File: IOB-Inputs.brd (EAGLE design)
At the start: 20.3 x 50.8 mm, 22 parts, among them J1 RJ12/6, Q0 P-FET, Q1 P-FET, Q2 P-FET, Q3 P-FET

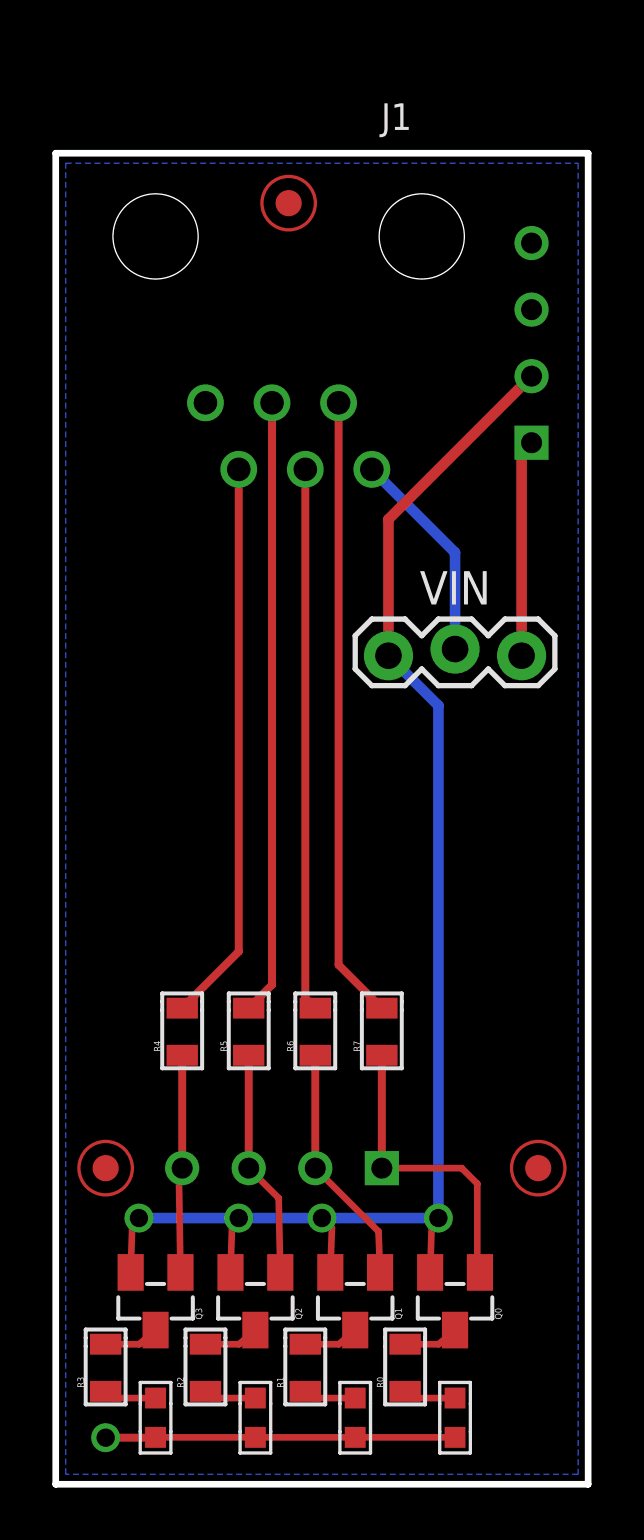
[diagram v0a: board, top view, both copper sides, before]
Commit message: added input protection diodes and RC filter to handle 1khz or less signals
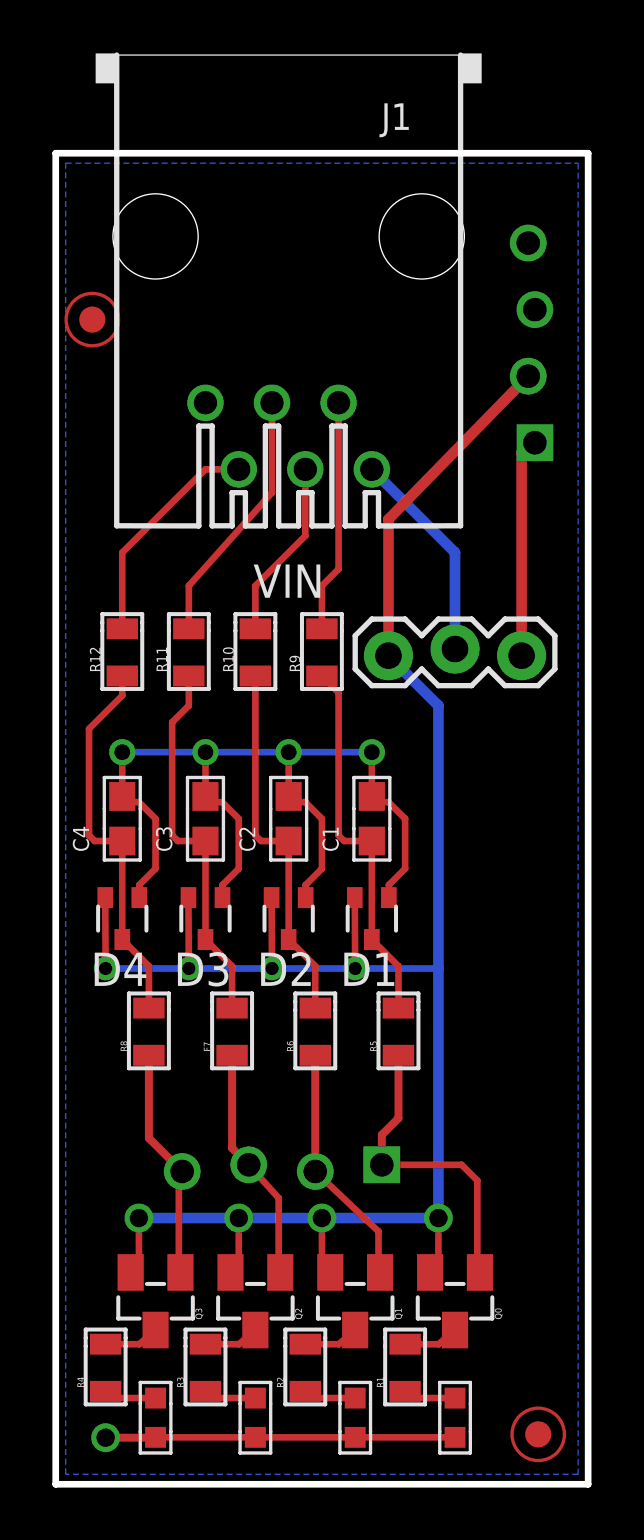
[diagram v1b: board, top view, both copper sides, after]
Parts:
- removed FID3: FIDUCIAL, SPCoast:FIDUCIAL_1MM
- removed LED0: Y, SPCoast:0603-LED
- removed R0: 2K0, SPCoast:0805-RES
- removed R7: 1K0, SPCoast:0805-RES
- added C1, C2, C3, C4: 0.01uF, SPCoast:0603-CAP
- added D1, D2, D3, D4: (no value), SPCoast:SOT323R
- added F7, R8: 1K0, SPCoast:0805-RES
- added LED4: Y, SPCoast:0603-LED
- added R10, R11, R12, R9: 82R, SPCoast:0805-RES
- IOB: value IO4-IOBBARE -> CONNECTOR-IO4-IOBBARE
- J1: device SPCoast:RJ25 -> SPCoast:RJ25-PANEL
- R4: value 1K0 -> 2K0
- moved R4 13.2 mm to (1.91, 4.45)
- moved FID2 10.2 mm to (18.4, 1.91)
- moved FID1 8.71 mm to (1.40, 44.5)
- moved R5 5.71 mm to (13.1, 17.3)
- moved LED1 3.81 mm to (15.2, 2.54)
- moved R1 3.81 mm to (13.3, 4.45)
- moved R2 3.81 mm to (9.53, 4.45)
- moved LED3 3.81 mm to (7.62, 2.54)
- moved LED2 3.81 mm to (11.4, 2.54)
- moved R3 3.81 mm to (5.71, 4.45)
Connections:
- removed net N$2 (its old number): LED0.A, R0.1
- new net N$10: C4.1, D4.2, R12.1, R8.2
- new net N$12: C3.1, D3.2, F7.2, R11.1
- new net N$13: C2.1, D2.2, R10.1, R6.2
- new net N$14: C1.1, D1.2, R5.2, R9.1
- new net N$5: LED4.A, R4.1
- net !IO1: now also R9.2; no longer R7.2
- net !IO2: now also R10.2; no longer R6.2
- net !IO3: now also R11.2; no longer R5.2
- net !IO4: now also R12.2; no longer R4.2
- net GND: now also C1.2, C2.2, C3.2, C4.2, D1.1, D2.1, D3.1, D4.1, LED4.C; no longer LED0.C
- net N$11: now also R1.2; no longer R0.2
- net N$30: now also R2.2; no longer R1.2
- net N$31: now also R3.2; no longer R2.2
- net N$32: now also R4.2; no longer R3.2
- net P1: now also R5.1; no longer R7.1
- net P3: now also F7.1; no longer R5.1
- net P4: now also R8.1; no longer R4.1
- net VCC: now also D1.3, D2.3, D3.3, D4.3
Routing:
- net GND: track 13.3 -> 49.2 mm, vias 1 -> 5
- net VCC: track 55.4 -> 79.2 mm, vias 4 -> 8
- net !IO1: track 23.8 -> 8.89 mm
- net N$10: track 0.00 -> 14.8 mm
- net N$14: track 0.00 -> 14.5 mm
- net N$12: track 0.00 -> 14.5 mm
- net N$13: track 0.00 -> 14.2 mm
- net !IO2: track 20.7 -> 6.87 mm
- net !IO3: track 23.5 -> 9.84 mm
- net !IO4: track 21.5 -> 8.67 mm
- net N$5: track 0.00 -> 2.01 mm
- net N$2 (its old number): track 2.01 -> 0.00 mm
- net P4: track 8.34 -> 8.97 mm
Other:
- board text added: "1.3"
- board text added: "Red Soldermask White Silkscreen"
- board text removed: "(aka 1.0C)"
- board text removed: "1.2"

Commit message: Panelized
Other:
- board text added: "C1"
- board text added: "C2"
- board text added: "C3"
- board text added: "C4"
- board text added: "D1"
- board text added: "D2"
- board text added: "D3"
- board text added: "D4"
- board text added: "F7"
- board text added: "J1"
- board text added: "Q0"
- board text added: "Q1"
- board text added: "Q2"
- board text added: "Q3"
- board text added: "R1"
- board text added: "R10"
- board text added: "R11"
- board text added: "R12"
- board text added: "R2"
- board text added: "R3"
- board text added: "R4"
- board text added: "R5"
- board text added: "R6"
- board text added: "R8"
- board text added: "R9"
- board text added: "VIN"

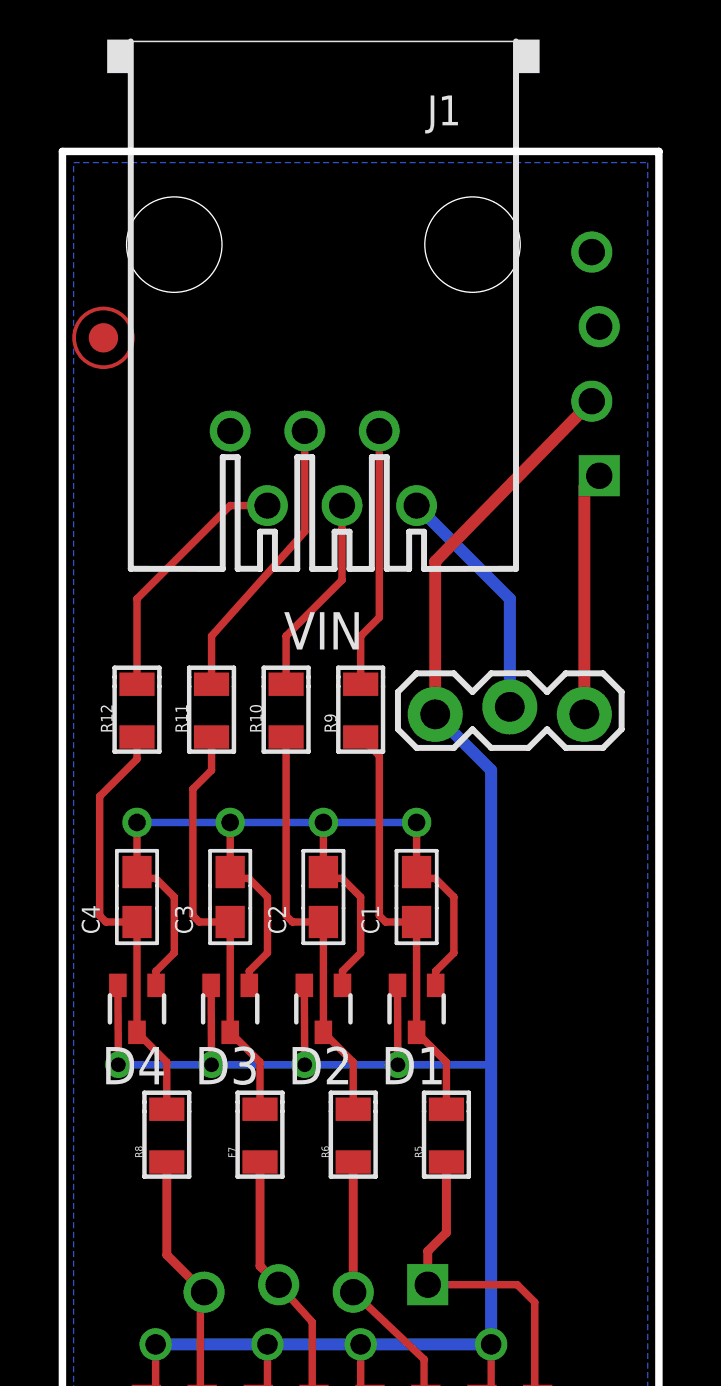
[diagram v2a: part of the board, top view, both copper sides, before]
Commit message: added 6x1 0.100 header
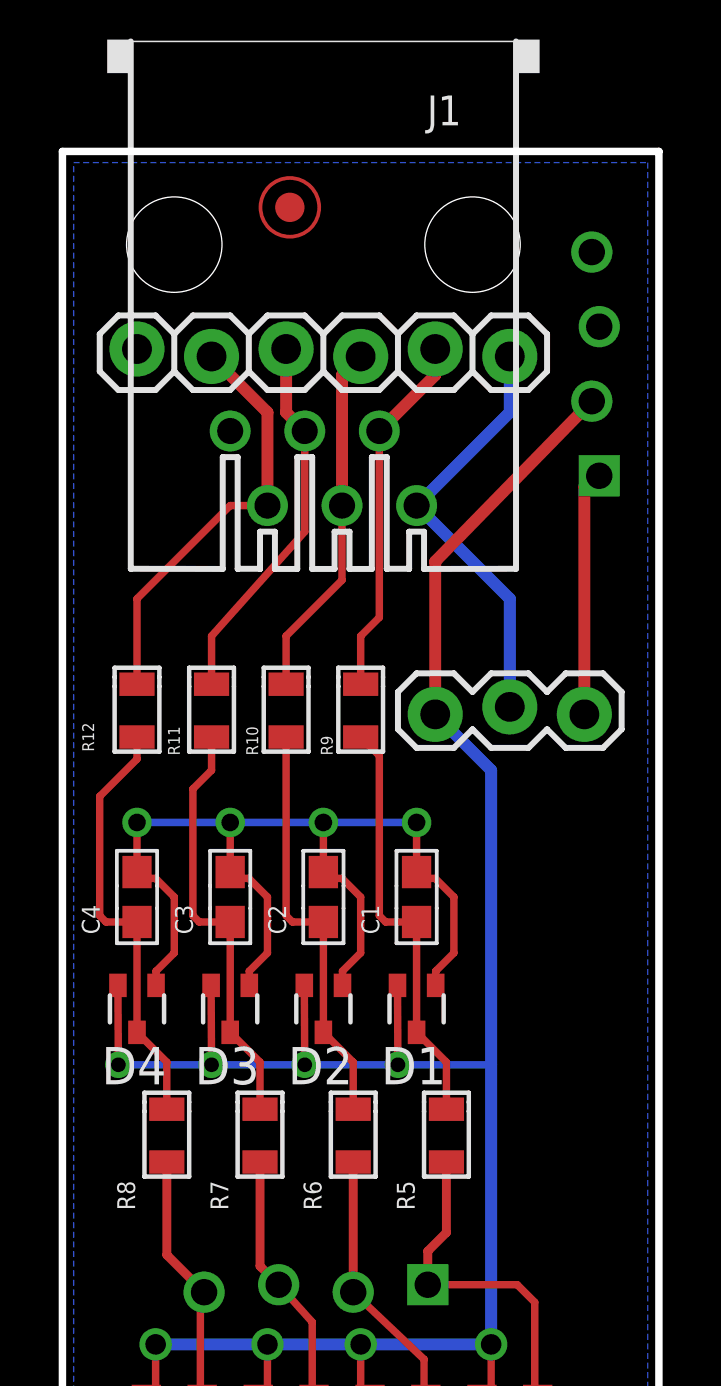
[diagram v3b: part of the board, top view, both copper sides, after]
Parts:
- added CON1: (no value), SPCoast:1X06_LOCK
- moved FID1 7.75 mm to (7.75, 48.9)
- renumbered F7 to R7
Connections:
- net !IO1: now also CON1.2
- net !IO2: now also CON1.3
- net !IO3: now also CON1.4
- net !IO4: now also CON1.5
- net GND: now also CON1.6
- net N$1: now also CON1.1
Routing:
- net N$1: track 8.17 -> 14.6 mm
- net !IO4: track 8.67 -> 14.5 mm
- net !IO2: track 6.87 -> 12.2 mm
- net !IO1: track 8.89 -> 12.5 mm
- net !IO3: track 9.84 -> 12.9 mm
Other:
- board text added: "1.4"
- board text added: "R7"
- board text removed: "1.3"
- board text removed: "F7"
- board text removed: "VIN"

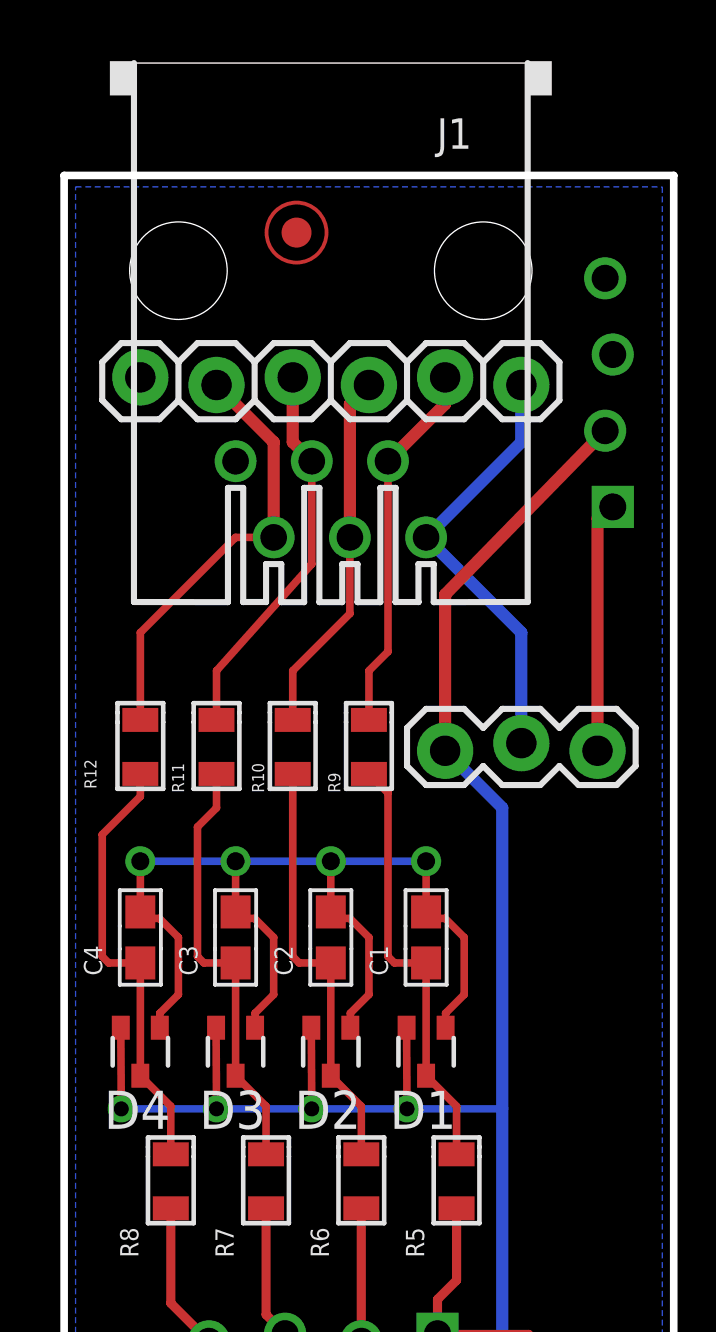
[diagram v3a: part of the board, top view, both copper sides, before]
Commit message: added 1x6 0.100 header
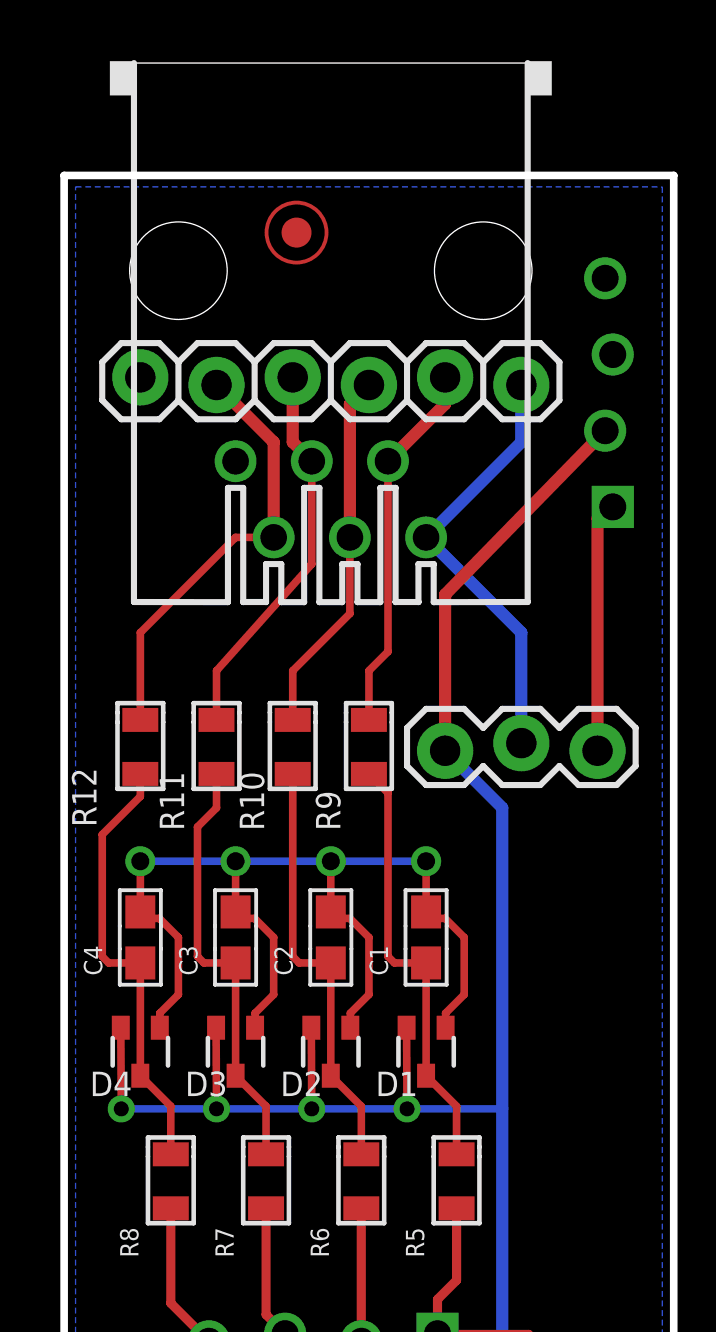
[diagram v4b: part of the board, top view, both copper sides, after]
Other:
- board text removed: "J1"
